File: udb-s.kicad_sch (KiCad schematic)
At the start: 10 parts, among them J1 TYPE-C-31-M-12, J2 78171-0004, U1 TPD4E05U06DQAR

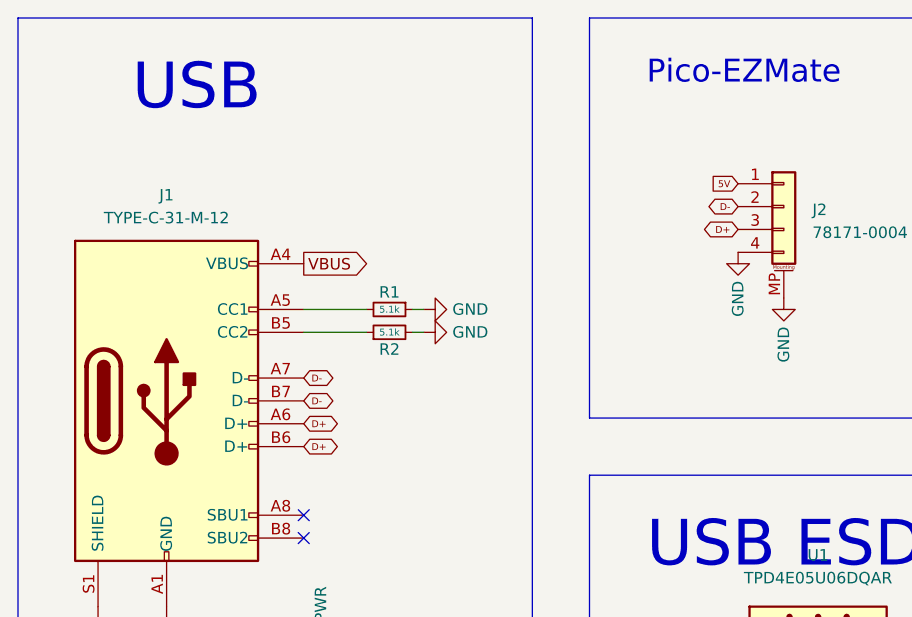
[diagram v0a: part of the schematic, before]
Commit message: Changed the Pinout of the ezMate connector. Added panelization with KiKit. 2x5 panels is about as small as possible for PCBA at JLCPCB, they want 70x70mm minimal size of the PCB. This means 50 PCBs is the MOQ with 5 panels.
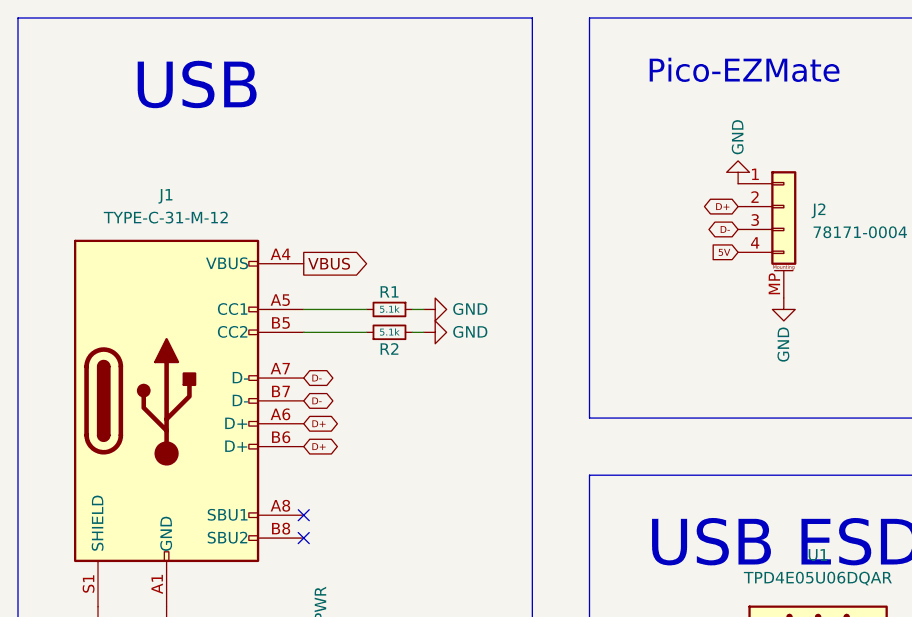
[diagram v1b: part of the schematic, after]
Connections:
- net 5V: now also J2.4 (Pin_4); no longer J2.1 (Pin_1)
- net D+: now also J2.2 (Pin_2); no longer J2.3 (Pin_3)
- net D-: now also J2.3 (Pin_3); no longer J2.2 (Pin_2)
- net GND: now also J2.1 (Pin_1); no longer J2.4 (Pin_4)
